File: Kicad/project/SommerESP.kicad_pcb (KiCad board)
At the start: 2 copper layers, 50.7 x 48.6 mm, 43 parts, among them J1 Serial programmer, J2 BRIDGE CONEX, J3 SOMMER CONEX BOARD, J4 SOMMER CONEX KEYPAD, J5 BRIDGE POWER, J6 SOMMER OUTPUT OC, Q1 STN3NF06, U2 G3VM-61D1, U3 G3VM-61D1, U4 LM2596SX-3.3/NOPB, U5 ESP32-C3-WROOM-02

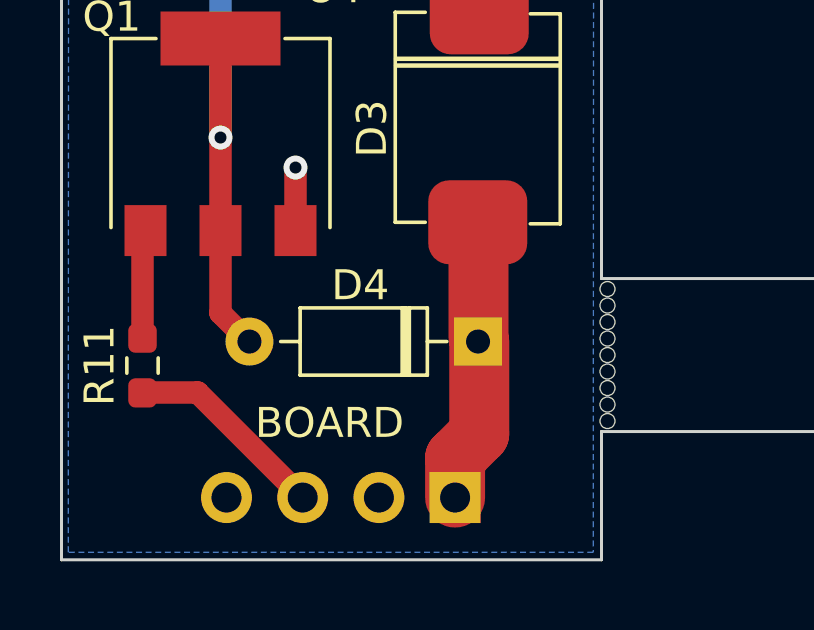
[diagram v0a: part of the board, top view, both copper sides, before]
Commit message: Found an error in the schematic for Diode D4. Was inverted in the schematic but correct in the PCB and Photos.
Thank you to Stefano Gnocato for pointing that out!
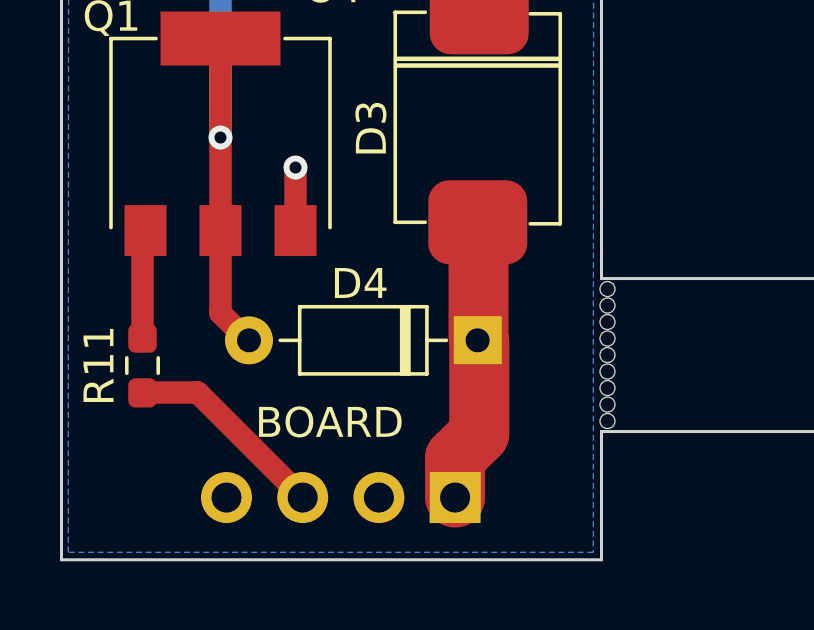
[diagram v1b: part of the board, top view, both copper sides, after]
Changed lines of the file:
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@@
   )
   (footprint "Diode_THT:D_DO-35_SOD27_P7.62mm_Horizontal" (layer "F.Cu")
-    (at 103.085 92.3 180)
+    (at 103.07 92.26 180)
     (descr "Diode, DO-35_SOD27 series, Axial, Horizontal, pin pitch=7.62mm, , length*diameter=4*2mm^2, , http://www.diodes.com/_files/packages/DO-35.pdf")
     (tags "Diode DO-35_SOD27 series Axial Horizontal pin pitch 7.62mm  length 4mm diameter 2mm")
     (property "Sheetfile" "SommerESP.kicad_sch")
     (property "Sheetname" "")
-    (property "ki_description" "Diode symbol for simulation only. Pin order incompatible with official kicad footprints")
-    (property "ki_keywords" "simulation")
+    (property "Sim.Device" "D")
+    (property "Sim.Pins" "1=K 2=A")
+    (property "ki_description" "100V 0.15A standard switching diode, DO-35")
+    (property "ki_keywords" "diode")
     (attr through_hole)
     (fp_text reference "D4" (at 3.925 1.875) (layer "F.SilkS")
@@
       (stroke (width 0.1) (type solid)) (layer "F.Fab"))
     (pad "1" thru_hole rect (at 0 0 180) (size 1.6 1.6) (drill 0.8) (layers "*.Cu" "*.Mask")
-      (net 10 "+24V") (pinfunction "K") (pintype "input"))
+      (net 10 "+24V") (pinfunction "K") (pintype "passive"))
     (pad "2" thru_hole oval (at 7.62 0 180) (size 1.6 1.6) (drill 0.8) (layers "*.Cu" "*.Mask")
-      (net 11 "AnalogSIG") (pinfunction "A") (pintype "input"))
+      (net 11 "AnalogSIG") (pinfunction "A") (pintype "passive"))
     (model "${KICAD6_3DMODEL_DIR}/Diode_THT.3dshapes/D_DO-35_SOD27_P7.62mm_Horizontal.wrl"
       (offset (xyz 0 0 0))

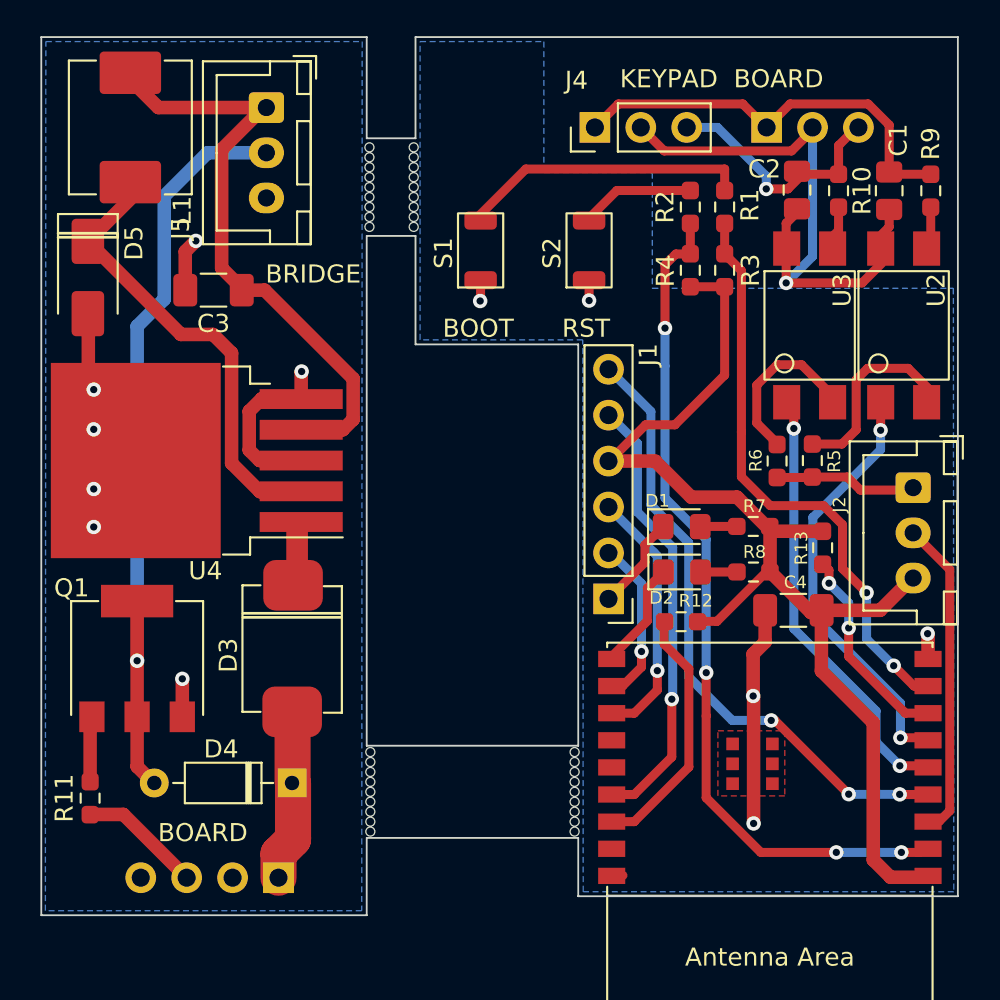
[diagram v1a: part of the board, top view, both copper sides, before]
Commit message: Updated Kicad to version 8 Added references to LCSC part numbers in the project and BOM Cleaned up a bit of silkscreen text and added some references Added JLCJLCJLCJLC on the silkscreen for the order number on JLC
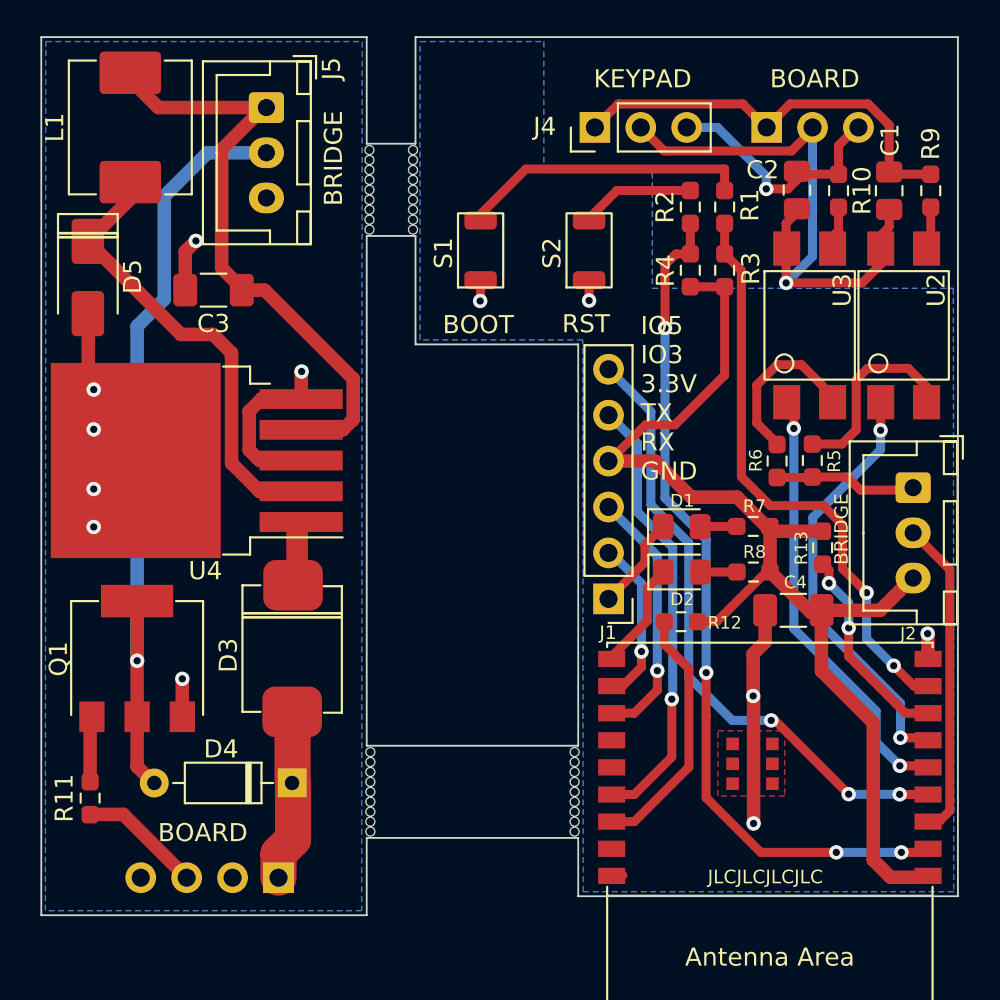
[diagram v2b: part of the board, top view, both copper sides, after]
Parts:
- moved REF** 0.16 mm to (109.8, 59.5)
- moved REF** 0.15 mm to (107.3, 59.5)
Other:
- outline, holes or cut-outs redrawn
- board text added: "JLCJLCJLCJLC"
- board text added: "SommerESP v1.1 Control board"
- board text added: "SommerESP v1.1 Power board"
- board text removed: "SommerESP v1 Control board"
- board text removed: "SommerESP v1 Power board"

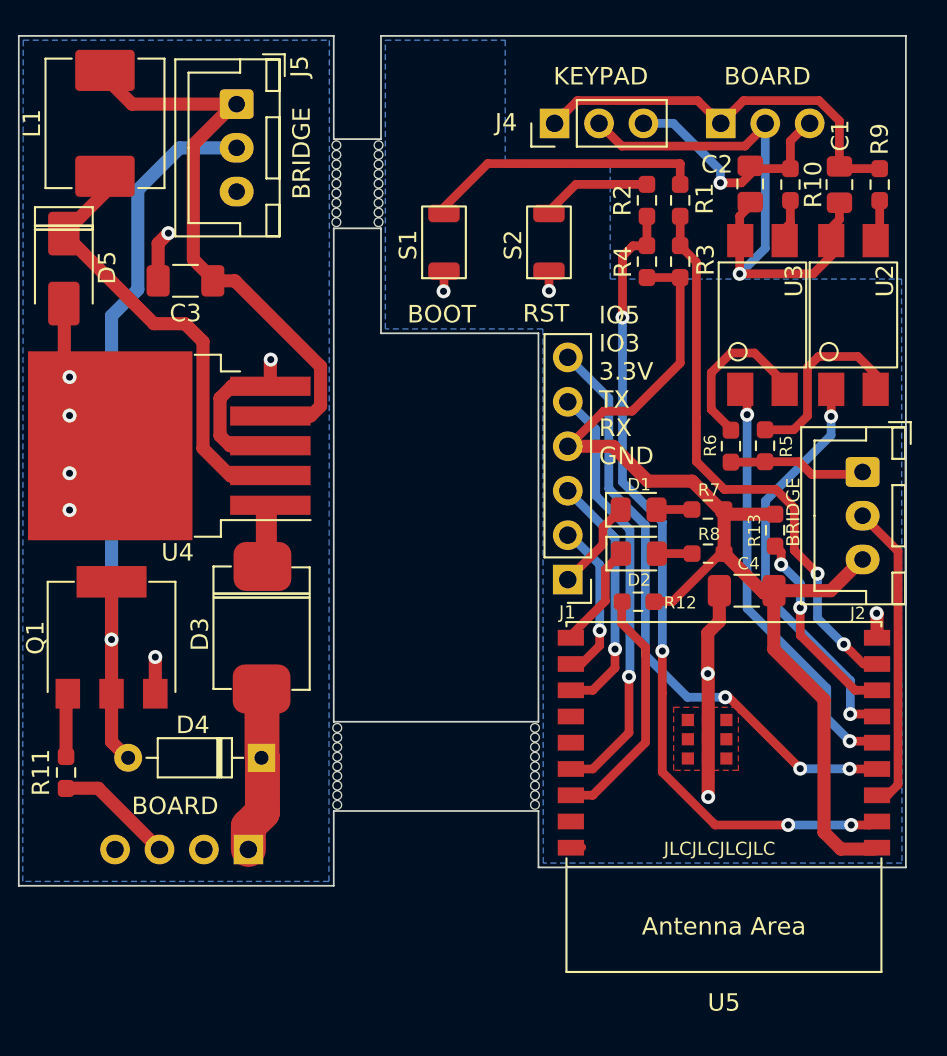
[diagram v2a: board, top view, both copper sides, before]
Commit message: Updated to V2. This is a transition version.
Updated yaml and added M3c4tr0x confirmation of
board working
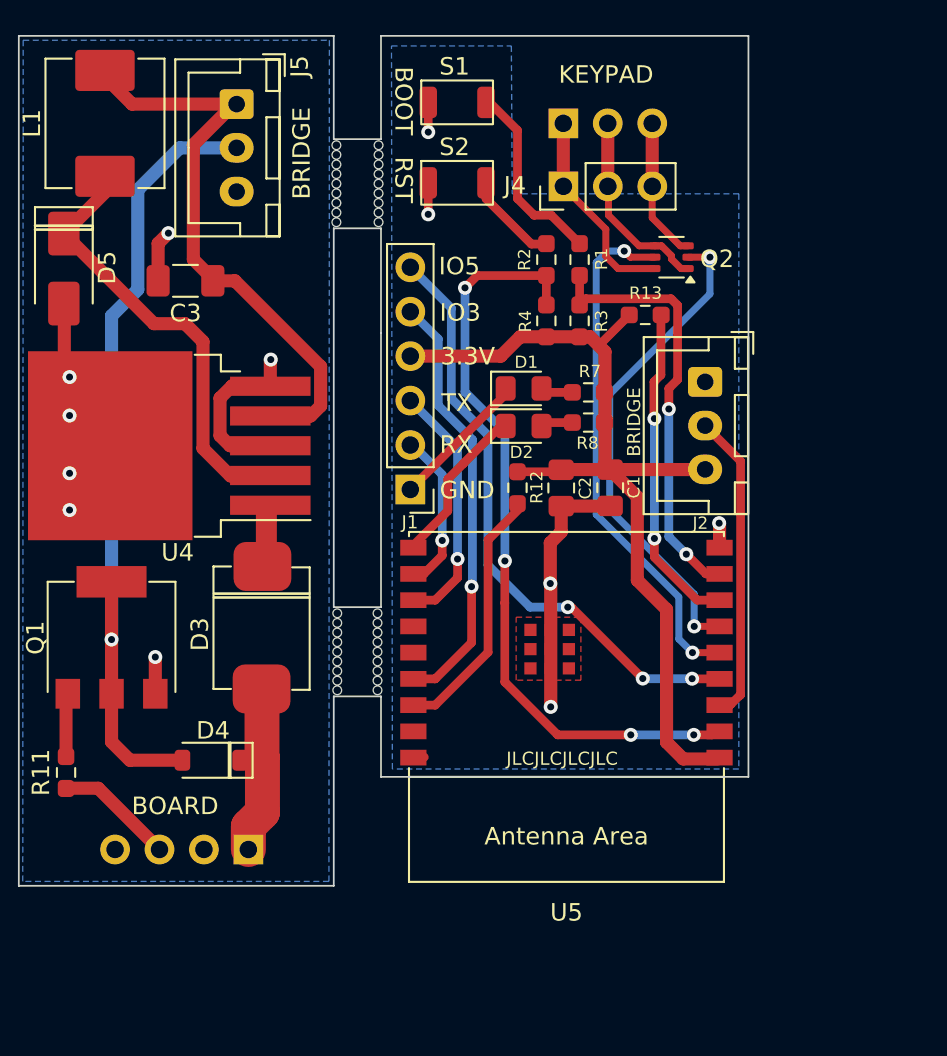
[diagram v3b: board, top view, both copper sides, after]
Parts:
- removed the C2 at (131.0, 59.5)
- removed R10, R9: 0603 100ohm, Resistor_SMD:R_0603_1608Metric_Pad0.98x0.95mm_HandSolder
- removed R5, R6: 0603 390, Resistor_SMD:R_0603_1608Metric_Pad0.98x0.95mm_HandSolder
- removed U2, U3: G3VM-61D1, CustomLibrary:G3VM-61D1
- added Q2: 2N7002DW, Package_TO_SOT_SMD:SOT-363_SC-70-6, F.Cu at (126.5, 63.6)
- C1: value 240 pf -> 0805 10uf
- C2: renamed from C4; value 1206 220uf -> 0805 100nf; footprint Capacitor_SMD:C_1206_3216Metric_Pad1.33x1.80mm_HandSolder -> Capacitor_SMD:C_0805_2012Metric_Pad1.18x1.45mm_HandSolder
- D1: value LED -> LED GREEN
- D2: value LED -> LED BLUE
- D4: footprint Diode_THT:D_DO-35_SOD27_P7.62mm_Horizontal -> Diode_SMD:D_SOD-123
- H1, H2, H3, H4: renamed from REF**; value Panelizing_1_1 -> MountingHole
- moved C1 21.7 mm to (123.0, 76.8)
- moved R13 14.4 mm to (125.0, 67.0), turned to 180 degrees
- moved C2 12.1 mm to (120.2, 76.8), turned to -90 degrees
- moved H4 11.1 mm to (109.7, 86.2)
- moved J1 10.4 mm to (111.6, 76.9)
- moved U5 10.4 mm to (120.5, 86.3)
- moved J2 10.4 mm to (128.4, 70.8)
- moved R8 10.1 mm to (121.8, 73.1)
- moved G*** 10.1 mm to (127.3, 85.2)
- moved D2 9.83 mm to (118.0, 73.3)
- moved R7 9.57 mm to (121.8, 71.4)
- moved D1 9.55 mm to (118.0, 71.2)
- moved R12 9.48 mm to (117.7, 76.8), turned to 90 degrees
- moved G*** 9.33 mm to (124.0, 64.3)
- moved J3 9.00 mm to (120.3, 56.0)
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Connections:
- C1 pad 1: Keypad1 -> +3.3VA
- C1 pad 2: Keypad2 -> GND2
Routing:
- net Keypad2: track 31.2 -> 11.0 mm, vias 1 -> 0
- net Keypad1: track 23.0 -> 11.4 mm
- net +3.3VA: track 63.3 -> 51.8 mm
- net Net-(U2-K): track 10.3 -> 0.00 mm
- net Net-(U3-K): track 8.88 -> 0.00 mm
- net IO9: track 32.2 -> 24.6 mm
- net IO8: track 11.3 -> 18.4 mm
- net IO6: track 23.3 -> 30.1 mm
- net Keypad3: track 13.8 -> 7.81 mm, vias 1 -> 0
- net IO7: track 23.3 -> 28.2 mm
- net Net-(R1-Pad1): track 15.6 -> 10.9 mm
- net EN: track 46.7 -> 43.1 mm
- net IO10: track 5.88 -> 8.99 mm
- net AnalogSIG: track 43.4 -> 46.3 mm
- net Net-(R9-Pad1): track 2.39 -> 0.00 mm
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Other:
- board size 50.7 x 48.6 mm -> 41.7 x 48.6 mm
- board text added: "3.3V"
- board text added: "GND"
- board text added: "IO3"
- board text added: "IO5"
- board text added: "RX"
- board text added: "SommerESP v2.0 Control board"
- board text added: "SommerESP v2.0 Power board"
- board text added: "TX"
- board text removed: "SommerESP v1.1 Control board"
- board text removed: "SommerESP v1.1 Power board"

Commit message: Version 3.0 of SommerESP
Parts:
- removed the G*** at (96.0, 83.3)
- removed H1, H2, H3, H4: MountingHole, CustomLibrary:Panelizing_1_1
- removed J2: BRIDGE CONEX, Connector_JST:JST_XH_B3B-XH-A_1x03_P2.50mm_Vertical
- removed J5: BRIDGE POWER, Connector_JST:JST_XH_B3B-XH-A_1x03_P2.50mm_Vertical
- added C4: 0805 22uf, Capacitor_SMD:C_0805_2012Metric_Pad1.18x1.45mm_HandSolder, F.Cu at (69.7, 40.1)
- D1: value LED GREEN -> LED Green
- D2: value LED BLUE -> LED Blue
- J1: footprint Connector_PinHeader_2.54mm:PinHeader_1x06_P2.54mm_Vertical -> Connector_PinHeader_2.54mm:PinHeader_1x08_P2.54mm_Vertical
- U4: value LM2596SX-3.3/NOPB -> LM2596SX-3.3/NOPB
- moved C1 93.4 mm to (44.5, 26.1), turned to 0 degrees
- moved R8 93.1 mm to (39.8, 28.9)
- moved C2 89.7 mm to (44.6, 28.6), turned to 0 degrees
- moved D2 88.9 mm to (39.8, 31.3), turned to 180 degrees
- moved R12 86.4 mm to (44.6, 30.8), turned to 180 degrees
- moved U5 85.7 mm to (47.8, 40.9)
- moved J1 82.4 mm to (35.6, 45.1)
- moved J4 78.7 mm to (49.1, 26.1)
- moved J3 76.0 mm to (49.1, 29.5)
- moved Q2 75.4 mm to (59.1, 30.0)
- moved J6 72.0 mm to (63.7, 36.7), turned to 0 degrees
- moved G*** 71.9 mm to (73.5, 37.5), turned to 180 degrees
- moved R13 71.1 mm to (60.0, 38.2), turned to -90 degrees
- moved D4 68.7 mm to (78.7, 27.1)
- moved R3 62.7 mm to (64.0, 41.9), turned to 90 degrees
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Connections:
- C1 pad 1: +3.3VA -> +3.3V
- C1 pad 2: GND2 -> GND
- C2 pad 1: +3.3VA -> +3.3V
- C2 pad 2: GND2 -> GND
- D1 pad 1: GND2 -> GND
- J1 pad 1: GND2 -> GND
- J1 pad 2: RX -> IO3
- J1 pad 3: TX -> IO19
- J1 pad 4: +3.3VA -> IO18
- J1 pad 5: IO3 -> TX
- J1 pad 6: IO5 -> RX
- R12 pad 2: +3.3VA -> +3.3V
- R13 pad 2: +3.3VA -> +3.3V
- R3 pad 2: +3.3VA -> +3.3V
- R4 pad 2: +3.3VA -> +3.3V
- R7 pad 1: +3.3VA -> +3.3V
- R8 pad 1: +3.3VA -> +3.3V
- S1 pad 2: GND2 -> GND
- S2 pad 2: GND2 -> GND
- U5 pad 1: +3.3VA -> +3.3V
- U5 pad 13: unconnected-(U5-GPIO18/USB_D--Pad13) -> IO18
- U5 pad 14: unconnected-(U5-GPIO19/USB_D+-Pad14) -> IO19
- U5 pad 19: GND2 -> GND
- U5 pad 3: ANALOGSIG2 -> AnalogSIG
- U5 pad 9: GND2 -> GND
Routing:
- net +3.3V: track 32.9 -> 120.3 mm, vias 0 -> 4
- net +3.3VA: track 51.8 -> 0.00 mm
- net GND2: track 27.1 -> 0.00 mm, vias 5 -> 0
- net EN: track 43.1 -> 17.5 mm, vias 4 -> 2
- net IO3: track 24.6 -> 3.58 mm, vias 1 -> 0
- net ANALOGSIG2: track 17.9 -> 0.00 mm
- net IO7: track 28.2 -> 12.9 mm, vias 2 -> 0
- net +24V: track 9.26 -> 24.2 mm, vias 0 -> 1
- net IO6: track 30.1 -> 15.3 mm
- net IO8: track 18.4 -> 5.27 mm
- net GND: track 19.4 -> 30.4 mm, vias 7 -> 15
- net TX: track 14.5 -> 4.35 mm, vias 1 -> 0
- net IO9: track 24.6 -> 15.1 mm
- net IO5: track 34.8 -> 26.1 mm, vias 3 -> 1
- net AnalogSIG: track 46.3 -> 37.6 mm, vias 1 -> 2
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- added copper zone on F.Cu, net GND
- removed copper zone on B.Cu, net GND2
- removed copper zone on F.Cu, net GND2
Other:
- board size 41.7 x 48.6 mm -> 76.8 x 23.5 mm
- board text added: ">"
- board text added: "IO18"
- board text added: "IO19"
- board text added: "POWER"
- board text added: "STATUS"
- board text added: "SommerESP V3"
- board text added: "SommerESP v3.0"
- board text removed: "BOARD"
- board text removed: "BRIDGE"
- board text removed: "IO5 IO3 3.3V TX RX GND"
- board text removed: "SommerESP v2.0 Control board"
- board text removed: "SommerESP v2.0 Power board"
